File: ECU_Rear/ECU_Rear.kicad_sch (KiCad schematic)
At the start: 2 parts, among them U1 YAAJ_DCDC_StepDown_LM2596, U2 ESP32-DevKitC

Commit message: Descrition
Fiz a descrição do trabalho feito até agora no projeto da placa ECU Rear.
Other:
- note added: "EMERGENCY FUEL SENSOR"
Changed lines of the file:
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@@
 (kicad_sch (version 20230121) (generator eeschema)
   (paper "A4")
+  (text "EMERGENCY FUEL SENSOR" (at 55.88 63.5 0)
+    (effects (font (size 1.5 1.5) (color 0 1 255 1)) (justify left bottom))
+  )
   (symbol (lib_id "StepDown_LM2596:YAAJ_DCDC_StepDown_LM2596") (at 105.41 100.33 0) (unit 1)
     (in_bom yes) (on_board yes) (dnp no) (fields_autoplaced)

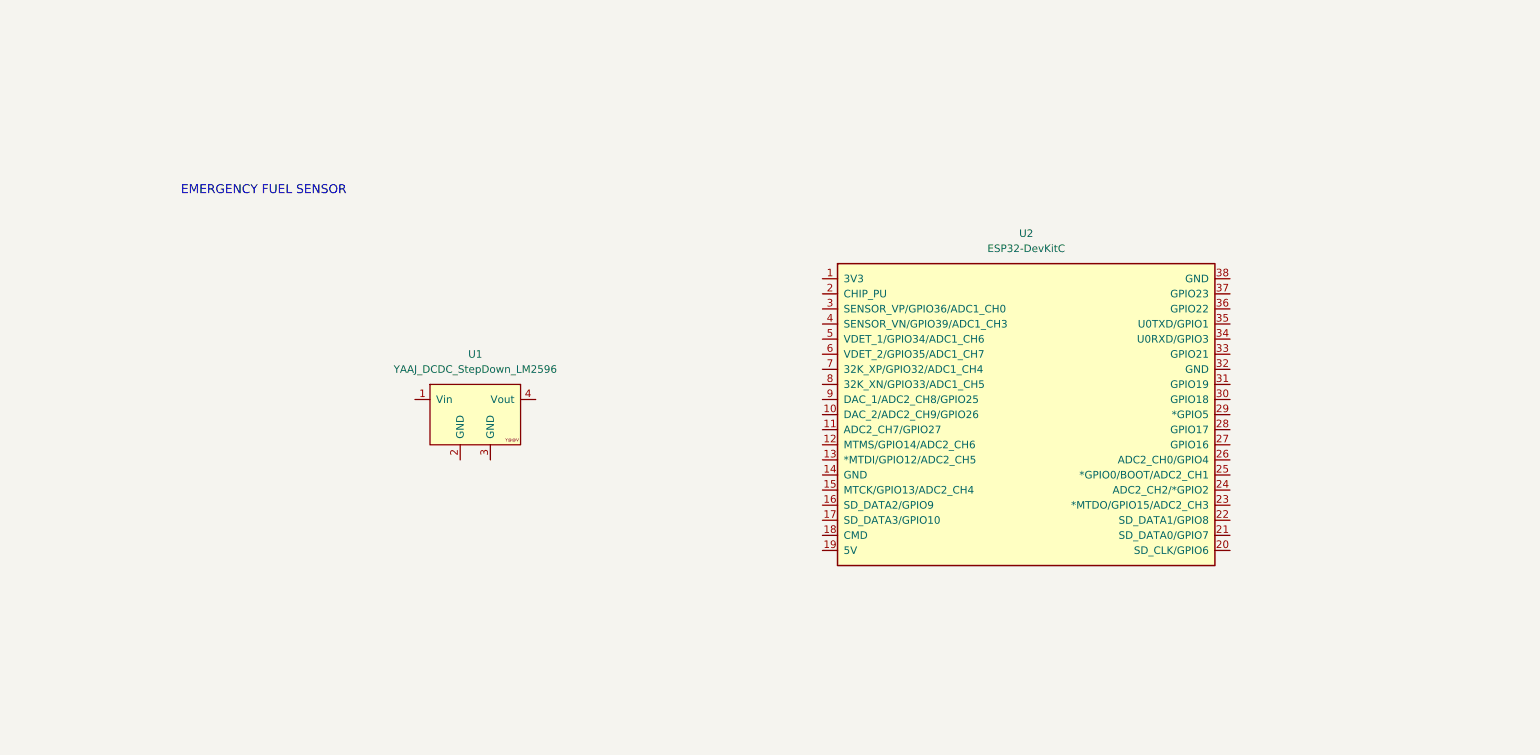
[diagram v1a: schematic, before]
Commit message: Esquemático da PCB da ECU rear
Por favor verificar se estão corretos os valores, principalmente os valores em POWER_SUPPLY dos capacitores e também o símbolo do capacitor polarizado. Encontrei apenas a versão "small". Também verificar os pinos da esp32, se estão corretos.
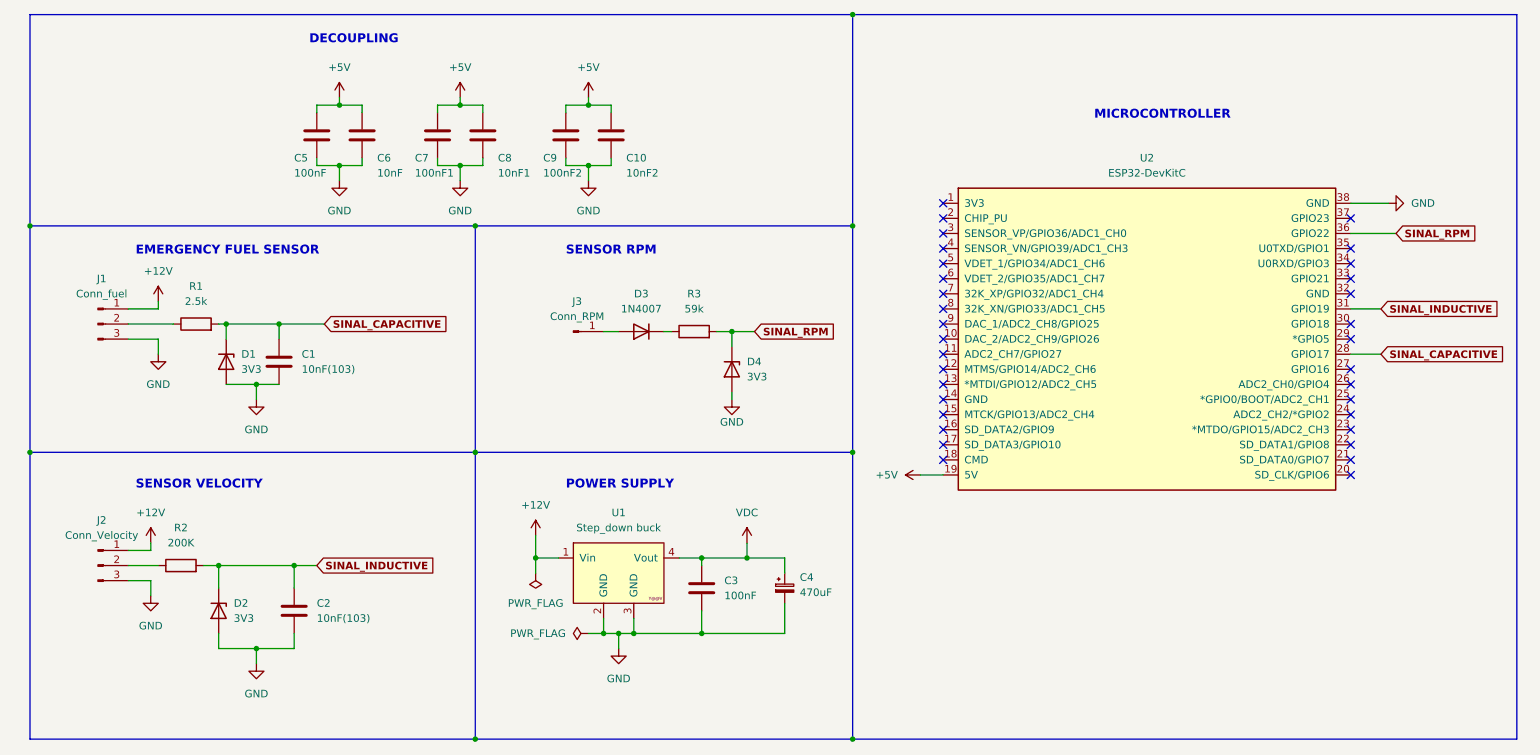
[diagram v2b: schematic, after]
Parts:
- added 100nF: C5, symbol Device:C
- added 100nF1: C7, symbol Device:C
- added 100nF2: C9, symbol Device:C
- added 10nF: C6, symbol Device:C
- added 10nF1: C8, symbol Device:C
- added 10nF2: C10, symbol Device:C
- added C1, C2: 10nF(103), symbol Device:C
- added C3: 100nF, symbol Device:C
- added C4: 470uF, symbol Device:C_Polarized_Small
- added D1, D2, D4: 3V3, symbol Device:D_Zener
- added D3: 1N4007, symbol Device:D
- added J1: Conn_fuel, symbol Connector:Conn_01x03_Pin
- added J2: Conn_Velocity, symbol Connector:Conn_01x03_Pin
- added J3: Conn_RPM, symbol Connector:Conn_01x01_Pin
- added R1: 2.5k, symbol Device:R
- added R2: 200K, symbol Device:R
- added R3: 59k, symbol Device:R
- U1: value YAAJ_DCDC_StepDown_LM2596 -> Step_down buck
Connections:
- net +12V: now reaches U1.1 (Vin)
- net +12V: now also J1.1 (Pin_1), J2.1 (Pin_1)
- net GND: now reaches U1.2 (GND)
- net GND: now also U1.3 (GND), U2.38 (GND), 100nF.2, 100nF1.2, 100nF2.2, 10nF.2, 10nF1.2, 10nF2.2, C1.2, C2.2, C3.2, C4.2, D1.2 (A), D2.2 (A), D4.2 (A), J1.3 (Pin_3), J2.3 (Pin_3)
- net VDC: now reaches U1.4 (Vout)
- net VDC: now also C3.1, C4.1
- net +5V: now reaches U2.19 (5V)
- net +5V: now also 100nF.1, 100nF1.1, 100nF2.1, 10nF.1, 10nF1.1, 10nF2.1
- net SINAL_CAPACITIVE: now reaches U2.28 (GPIO17)
- net SINAL_CAPACITIVE: now also C1.1, D1.1 (K), R1.2
- net SINAL_INDUCTIVE: now reaches U2.31 (GPIO19)
- net SINAL_INDUCTIVE: now also C2.1, D2.1 (K), R2.2
- net SINAL_RPM: now reaches U2.36 (GPIO22)
- net SINAL_RPM: now also D4.1 (K), R3.2
- new net: D3.1 (K), R3.1
- new net: D3.2 (A), J3.1 (Pin_1)
- new net: J2.2 (Pin_2), R2.1
- new net: J1.2 (Pin_2), R1.1
- no-connect marks 0 -> 33
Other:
- note added: "DECOUPLING"
- note added: "MICROCONTROLLER"
- note added: "POWER SUPPLY"
- note added: "SENSOR RPM"
- note added: "SENSOR VELOCITY"
- moved on the sheet: U1, U2

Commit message: Adicionei 1 optoacoplador
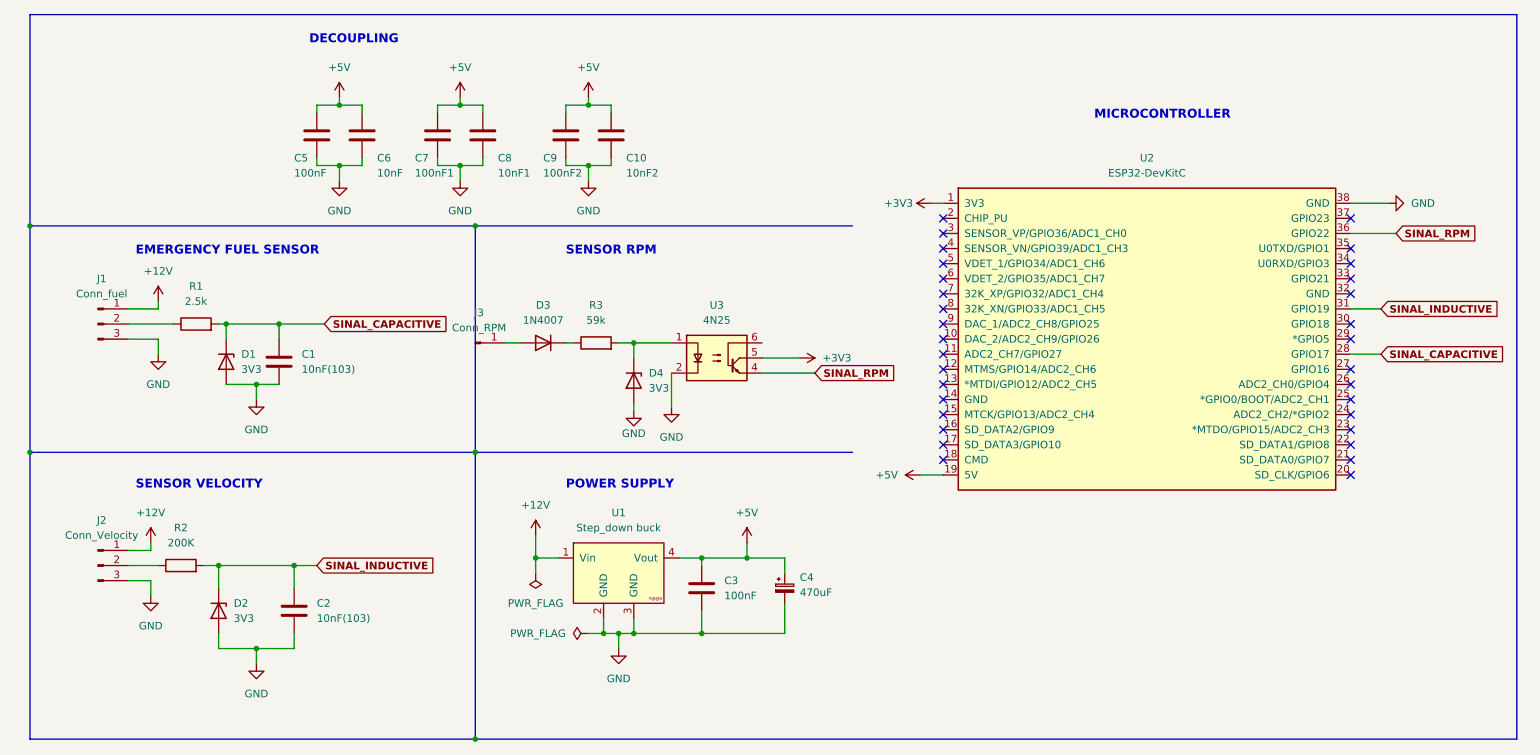
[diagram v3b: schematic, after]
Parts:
- added U3: 4N25, Package_DIP:DIP-6_W7.62mm, symbol Isolator:4N25
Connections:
- net VDC is gone; now on net +5V: C3.1, C4.1, U1.4 (Vout)
- net GND: now also U3.2
- net SINAL_RPM: now also U3.4; no longer D4.1 (K), R3.2
- net +3V3: now reaches U2.1 (3V3)
- net +3V3: now also U3.5
- new net: D4.1 (K), R3.2, U3.1
- no-connect marks 33 -> 32
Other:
- moved on the sheet: D3, D4, J3, R3

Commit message: Terminei o esquemático, vou começar a placa segunda dia 14/08
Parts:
- removed C1: 10nF(103), symbol Device:C
- removed D1: 3V3, symbol Device:D_Zener
- removed J1: Conn_fuel, symbol Connector:Conn_01x03_Pin
- removed R1: 2.5k, symbol Device:R
- C10: renamed from 10nF2; value C10 -> 10nF
- C5: renamed from 100nF; value C5 -> 100nF
- C6: renamed from 10nF; value C6 -> 10nF
- C7: renamed from 100nF1; value C7 -> 100nF
- C8: renamed from 10nF1; value C8 -> 10nF
- C9: renamed from 100nF2; value C9 -> 100nF

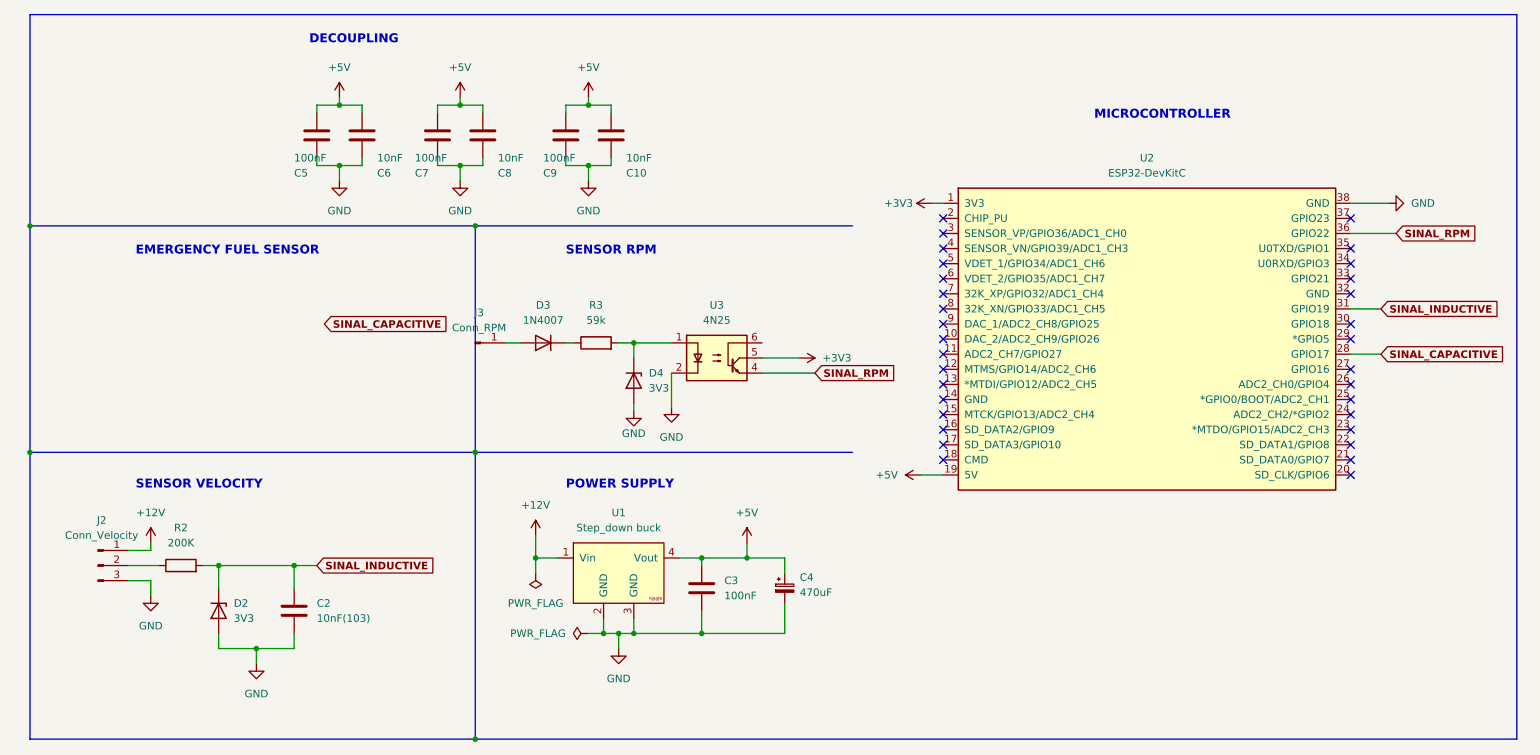
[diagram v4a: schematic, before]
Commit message: adicionei os aptoacopladores aos circuitos dos sensores da PCB
.
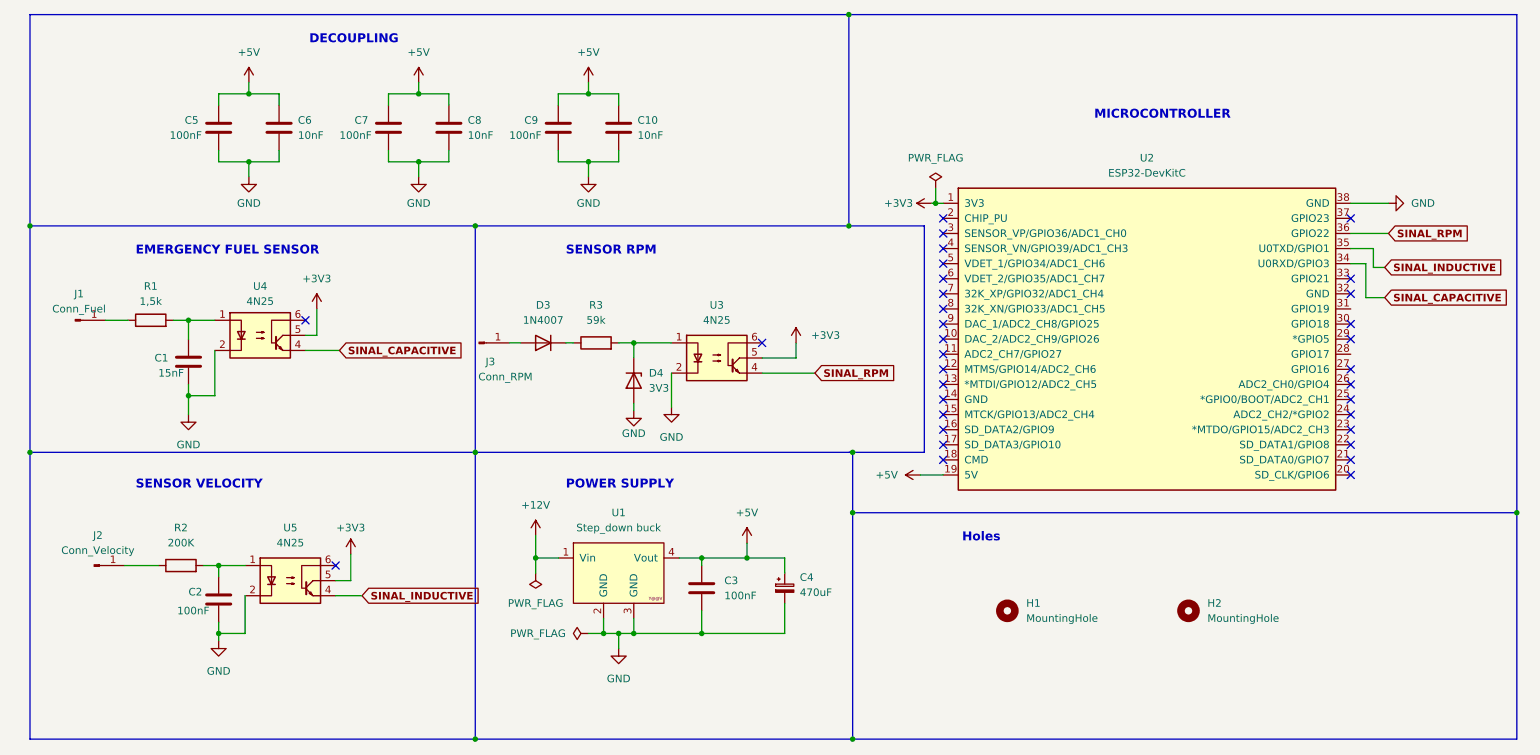
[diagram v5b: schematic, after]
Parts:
- removed D2: 3V3, symbol Device:D_Zener
- removed J2: Conn_Velocity, symbol Connector:Conn_01x03_Pin
- added C1: 15nF, symbol Device:C
- added H1, H2: MountingHole, symbol Mechanical:MountingHole
- added J1: Conn_Fuel, symbol Connector:Conn_01x01_Pin
- added J2: Conn_Velocity, symbol Connector:Conn_01x01_Pin
- added R1: 1,5k, symbol Device:R
- added U4, U5: 4N25, Package_DIP:DIP-6_W7.62mm, symbol Isolator:4N25
- C2: value 10nF(103) -> 100nF
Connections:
- net +3V3: now also U4.5, U5.5
- net GND: now also C1.2, U4.2, U5.2
- net SINAL_CAPACITIVE: now also U2.34 (U0RXD/GPIO3), U4.4; no longer U2.28 (GPIO17)
- net SINAL_INDUCTIVE: now also U2.35 (U0TXD/GPIO1), U5.4; no longer C2.1, R2.2, U2.31 (GPIO19)
- net at R2.1: now also J2.1 (Pin_1)
- new net: C1.1, R1.2, U4.1
- new net: C2.1, R2.2, U5.1
- new net: J1.1 (Pin_1), R1.1
- no-connect marks 32 -> 33
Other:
- note added: "Holes"
- moved on the sheet: J3

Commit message: Esquemático e Desenho da placa
Fiz modificações nos Decoupling. Colocando os números corretos de componentes e próximos às saídas de energia.  Iniciei o desenho da placa levando em consideração as dimensões da caixa e a melhor posição do esp32.
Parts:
- removed J1: Conn_Fuel, symbol Connector:Conn_01x01_Pin
- removed J2: Conn_Velocity, symbol Connector:Conn_01x01_Pin
- removed J3: Conn_RPM, symbol Connector:Conn_01x01_Pin
- added J1: Conn_01x02_Pin, symbol Connector:Conn_01x02_Pin
- added J4: Conn_01x03_Pin, Connector_PinHeader_2.54mm:PinHeader_1x03_P2.54mm_Vertical, symbol Connector:Conn_01x03_Pin
- C1, C10, C2, C3, C4, C5, C6, C7, C8, C9: footprint (none) -> Capacitor_THT:C_Disc_D5.0mm_W2.5mm_P5.00mm
- D3: footprint (none) -> Diode_THT:D_A-405_P7.62mm_Horizontal
- D4: value 3V3 -> ZENER 3V3; footprint (none) -> Diode_THT:D_A-405_P7.62mm_Horizontal
- H1, H2: footprint (none) -> MountingHole:MountingHole_4.3mm_M4
- R1, R2, R3: footprint (none) -> Resistor_THT:R_Axial_DIN0204_L3.6mm_D1.6mm_P5.08mm_Horizontal
- U1: footprint (none) -> StepDown:StepDown_LM2596
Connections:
- net +3V3: now also C7.1, C8.1
- net +5V: no longer C7.1, C8.1
- net CONN_RPM: now reaches D3.2 (A)
- net CONN_RPM: now also J4.3 (Pin_3)
- net CONN_INDUCTIVE: now reaches R2.1
- net CONN_INDUCTIVE: now also J4.2 (Pin_2)
- net SIGNAL_CAPACITIVE: now reaches U2.4 (SENSOR_VN/GPIO39/ADC1_CH3)
- net SIGNAL_CAPACITIVE: now also U4.4
- net SIGNAL_INDUCTIVE: now reaches U2.5 (VDET_1/GPIO34/ADC1_CH6)
- net SIGNAL_INDUCTIVE: now also U5.4
- net SIGNAL_RPM: now reaches U2.6 (VDET_2/GPIO35/ADC1_CH7)
- net SIGNAL_RPM: now also U3.4
- net CONN_CAPACITIVE: now reaches R1.1
- net CONN_CAPACITIVE: now also J4.1 (Pin_1)
- net +12V renamed CONN_12V
- net CONN_12V: now also J1.1 (Pin_1)
- net SINAL_CAPACITIVE: no longer names the net of U2.34 (U0RXD/GPIO3)
- net SINAL_CAPACITIVE: no longer U4.4
- net SINAL_INDUCTIVE: no longer names the net of U2.35 (U0TXD/GPIO1)
- net SINAL_INDUCTIVE: no longer U5.4
- net SINAL_RPM: no longer names the net of U2.36 (GPIO22)
- net SINAL_RPM: no longer U3.4
- no-connect marks 33 -> 35
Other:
- note added: "CONNECTIONS"
- note added: "MOUNTING"
- note removed: "Holes"
- moved on the sheet: C1, C2, C3, C4, D3, D4, H1, H2, R1, R2, R3, U1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

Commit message: fiz schematic and remake layout
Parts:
- added C11: 15nF, Capacitor_THT:C_Disc_D5.0mm_W2.5mm_P5.00mm, symbol Device:C
- C2: value 100nF -> 15nF
- J1: value Conn_01x02_Pin -> Conn_PWR_IN; footprint (none) -> Connector_PinHeader_2.54mm:PinHeader_1x02_P2.54mm_Vertical
- J4: value Conn_01x03_Pin -> Conn_SENSORS
- R1: value 1,5k -> 200k
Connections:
- net +3V3: now also C10.1, C9.1; no longer C7.1, C8.1
- net +5V: now also C7.1, C8.1; no longer C10.1, C5.1, C6.1, C9.1
- net GND: now also J1.2 (Pin_2), U2.14 (GND), U2.32 (GND), C11.2
- net at D4.1 (K), R3.2, U3.1: now also C11.1
- net CONN_12V renamed +12V
- net +12V: now also C5.1, C6.1
- no-connect marks 35 -> 33
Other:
- company: (none) -> Parahybaja
- title: (none) -> ECU Rear
- moved on the sheet: C2, C3, C4, D3, D4, H1, H2, J1, J4, R2, R3, U1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

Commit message: ECU_DISPLAY First project
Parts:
- C4: footprint Capacitor_THT:C_Disc_D5.0mm_W2.5mm_P5.00mm -> Capacitor_THT:CP_Radial_D6.3mm_P2.50mm
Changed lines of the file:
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@@
       (effects (font (size 1.27 1.27)) (justify left))
     )
-    (property "Footprint" "Capacitor_THT:C_Disc_D5.0mm_W2.5mm_P5.00mm" (at 163.83 133.35 0)
+    (property "Footprint" "Capacitor_THT:CP_Radial_D6.3mm_P2.50mm" (at 163.83 133.35 0)
       (effects (font (size 1.27 1.27)) hide)
     )
